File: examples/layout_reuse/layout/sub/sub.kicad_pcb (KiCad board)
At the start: 2 copper layers, 3 parts

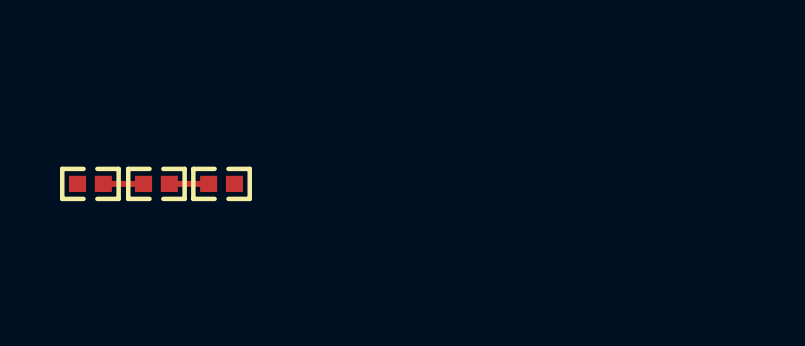
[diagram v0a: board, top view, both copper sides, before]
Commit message: Speed: Rewrite dataclass parser in Zig (#1427)
# Rewrite kicad fileformat stuff

Rewrite sexp format definition in zig.
Improve architecture of fileformat access by a lot.
Changed a lot of pcb sync logic along the way.

---------

Co-authored-by: Sam Mellor <sam@atopile.io>
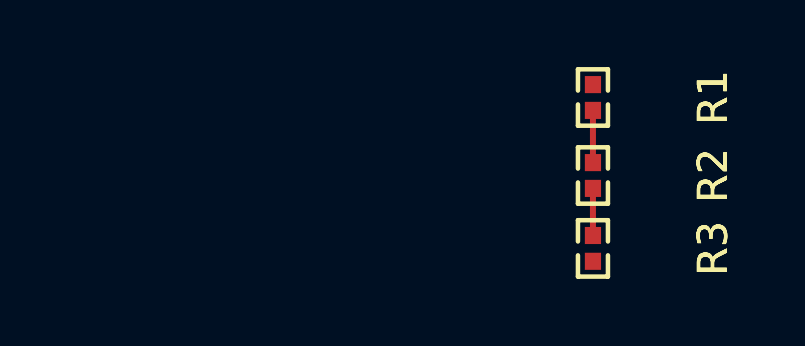
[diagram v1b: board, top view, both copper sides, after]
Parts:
- moved R1 17.0 mm to (56.4, 46.9), turned to -90 degrees
- moved R2 14.6 mm to (56.4, 49.5), turned to -90 degrees
- moved R3 12.6 mm to (56.4, 52.0), turned to -90 degrees
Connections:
- net -net-0 renamed footprint-net-1
- net -net-1 renamed footprint-net-2
- net r_chain[0]-net renamed footprint-net-0
- net r_chain[2]-net renamed footprint-net-3

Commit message: update examples
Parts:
- R1, R2, R3: value 1kΩ ±1% 62.5mW -> {1000.0±1.0%}Ω
- moved R2 89.5 mm to (0.00, -20.0), turned to 0 degrees
- moved R3 83.7 mm to (0.00, -10.0), turned to 0 degrees
- moved R1 73.3 mm to (0.00, 0.00), turned to 0 degrees
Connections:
- net footprint-net-0 renamed r_chain[0].unnamed[0]-unnamed[0]
- net footprint-net-1 renamed unnamed[0]-0
- net footprint-net-2 renamed unnamed[0]-1
- net footprint-net-3 renamed unnamed[1]
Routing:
- net unnamed[0]-0: track 1.74 -> 0.00 mm
- net r_chain[0].unnamed[0]-unnamed[0]: track 0.00 -> 1.74 mm
